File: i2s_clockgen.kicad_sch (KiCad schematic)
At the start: 4 parts, among them U21 24.576MHz, U27 4040

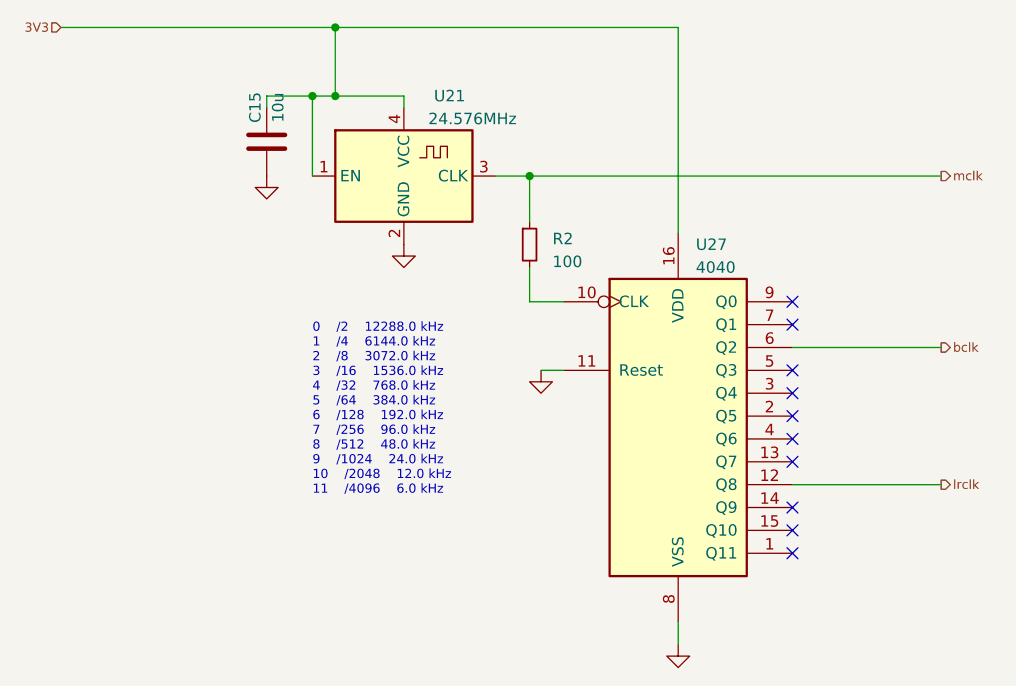
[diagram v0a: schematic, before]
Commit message: update to kicad 8
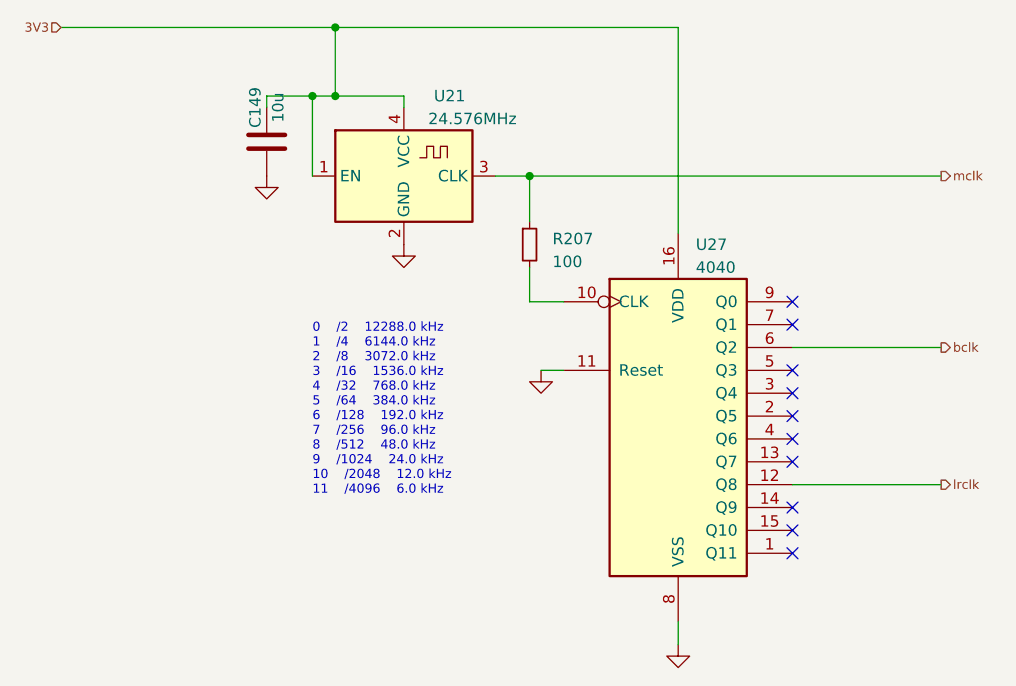
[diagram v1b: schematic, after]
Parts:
- renumbered C15 to C149, R2 to R207

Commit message: updates
* add line out
* fix almost all erc
* some more random edits
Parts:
- U21: PN (none) -> KC2016K24.57C10E
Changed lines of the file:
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@@
 			)
 		)
-		(property "PN" ""
+		(property "PN" "KC2016K24.57C10E"
 			(at 69.85 55.88 0)
 			(effects

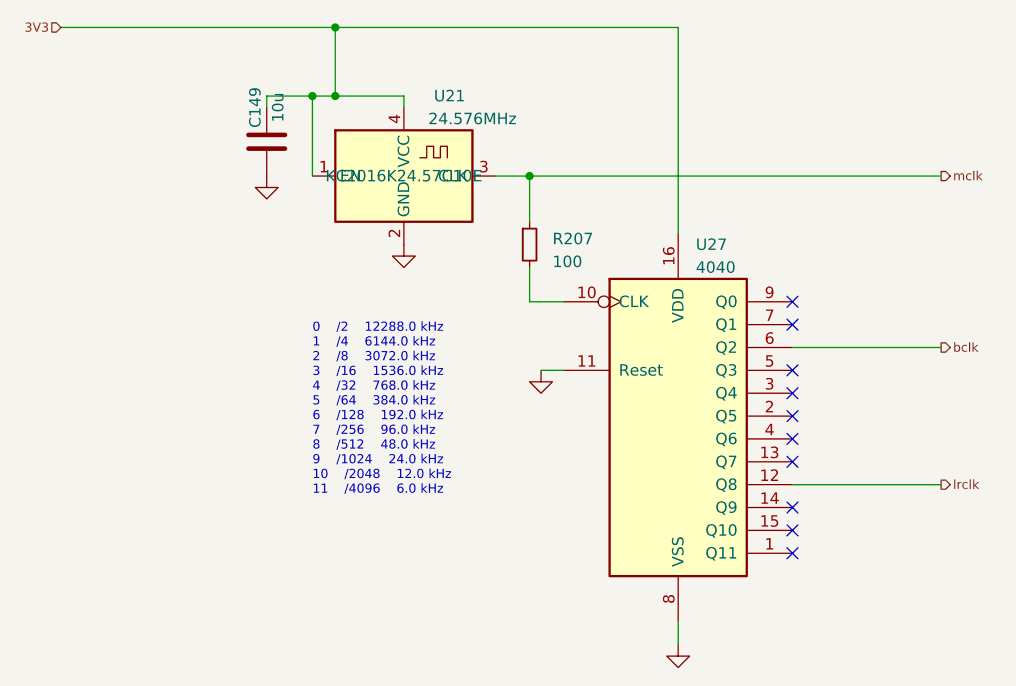
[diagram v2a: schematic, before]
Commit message: add power input +...
+ tons of fixes, footprint assignments, etc
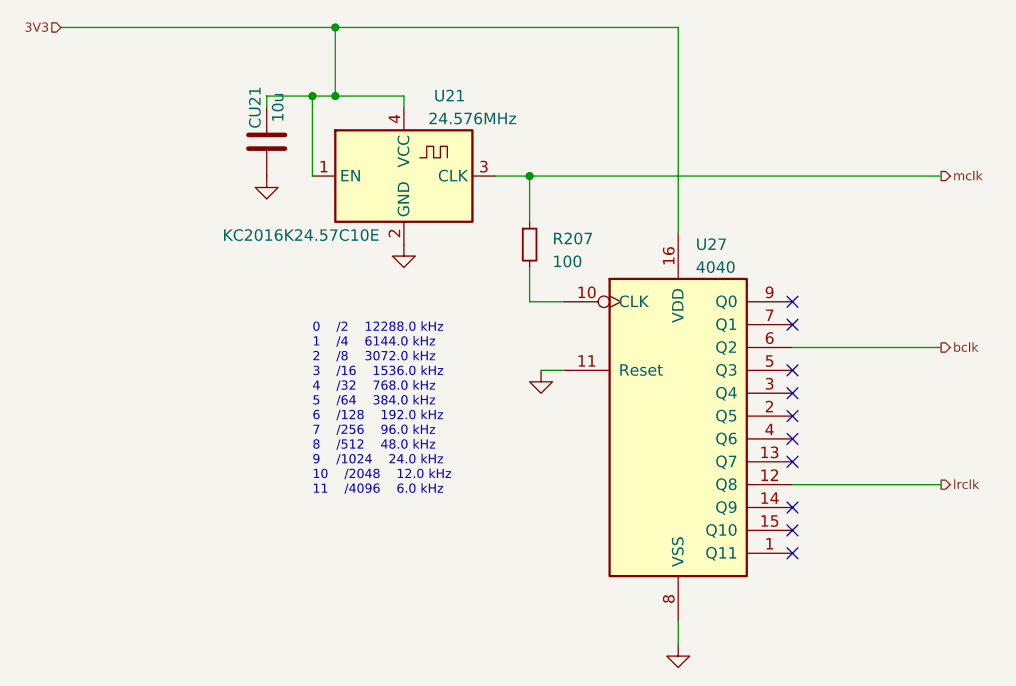
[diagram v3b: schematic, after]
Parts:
- U21: footprint (none) -> invendelirium_audio:K2016_kyocera_xosc
- renumbered C149 to CU21
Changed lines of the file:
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@@
+			)
+		)
+		(property "Sim.Device" ""
+			(at 83.82 63.5 0)
+			(effects
+				(font
+					(size 1.27 1.27)
+				)
+				(hide yes)
+			)
+		)
+		(property "Sim.Library" ""
+			(at 83.82 63.5 0)
+			(effects
+				(font
+					(size 1.27 1.27)
+				)
+				(hide yes)
+			)
+		)
+		(property "Sim.Name" ""
+			(at 83.82 63.5 0)
+			(effects
+				(font
+					(size 1.27 1.27)
+				)
+				(hide yes)
+			)
+		)
+		(property "Sim.Pins" ""
+			(at 83.82 63.5 0)
+			(effects
+				(font
+					(size 1.27 1.27)
+				)
+				(hide yes)
 			)
 		)
@@
 		(on_board yes)
 		(dnp no)
-		(property "Reference" "C149"
+		(property "Reference" "CU21"
 			(at 53.34 48.26 90)
 			(effects
@@
 		)
 		(property "Voltage" "16V"
+			(at 54.61 52.07 0)
+			(effects
+				(font
+					(size 1.27 1.27)
+				)
+				(hide yes)
+			)
+		)
+		(property "Sim.Device" ""
+			(at 54.61 52.07 0)
+			(effects
+				(font
+					(size 1.27 1.27)
+				)
+				(hide yes)
+			)
+		)
+		(property "Sim.Library" ""
+			(at 54.61 52.07 0)
+			(effects
+				(font
+					(size 1.27 1.27)
+				)
+				(hide yes)
+			)
+		)
+		(property "Sim.Name" ""
+			(at 54.61 52.07 0)
+			(effects
+				(font
+					(size 1.27 1.27)
+				)
+				(hide yes)
+			)
+		)
+		(property "Sim.Pins" ""
 			(at 54.61 52.07 0)
 			(effects
@@
 			(project "uberamp1"
 				(path "/310059c1-d84b-43e2-9c9a-0e426c534a12/2fefbd12-b9e0-4841-863e-105a3ff6cb21"
-					(reference "C149")
+					(reference "CU21")
 					(unit 1)
 				)
@@
 			)
 		)
+		(property "Sim.Device" ""
+			(at 100.33 82.55 0)
+			(effects
+				(font
+					(size 1.27 1.27)
+				)
+				(hide yes)
+			)
+		)
+		(property "Sim.Library" ""
+			(at 100.33 82.55 0)
+			(effects
+				(font
+					(size 1.27 1.27)
+				)
+				(hide yes)
+			)
+		)
+		(property "Sim.Name" ""
+			(at 100.33 82.55 0)
+			(effects
+				(font
+					(size 1.27 1.27)
+				)
+				(hide yes)
+			)
+		)
+		(property "Sim.Pins" ""
+			(at 100.33 82.55 0)
+			(effects
+				(font
+					(size 1.27 1.27)
+				)
+				(hide yes)
+			)
+		)
 		(pin "1"
 		)
@@
 			)
 		)
-		(property "Footprint" ""
+		(property "Footprint" "invendelirium_audio:K2016_kyocera_xosc"
 			(at 73.66 52.07 0)
 			(effects
@@
 		)
 		(property "PN" "KC2016K24.57C10E"
+			(at 58.42 62.484 0)
+			(effects
+				(font
+					(size 1.27 1.27)
+				)
+			)
+		)
+		(property "Sim.Device" ""
 			(at 69.85 55.88 0)
 			(effects
@@
 					(size 1.27 1.27)
 				)
-			)
-		)
+				(hide yes)
+			)
+		)
+		(property "Sim.Library" ""
+			(at 69.85 55.88 0)
+			(effects
+				(font
+					(size 1.27 1.27)
+				)
+				(hide yes)
+			)
+		)
+		(property "Sim.Name" ""
+			(at 69.85 55.88 0)
+			(effects
+				(font
+					(size 1.27 1.27)
+				)
+				(hide yes)
+			)
+		)
+		(property "Sim.Pins" ""
+			(at 69.85 55.88 0)
+			(effects
+				(font
+					(size 1.27 1.27)
+				)
+				(hide yes)
+			)
+		)

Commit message: update partnumbers to what was bought
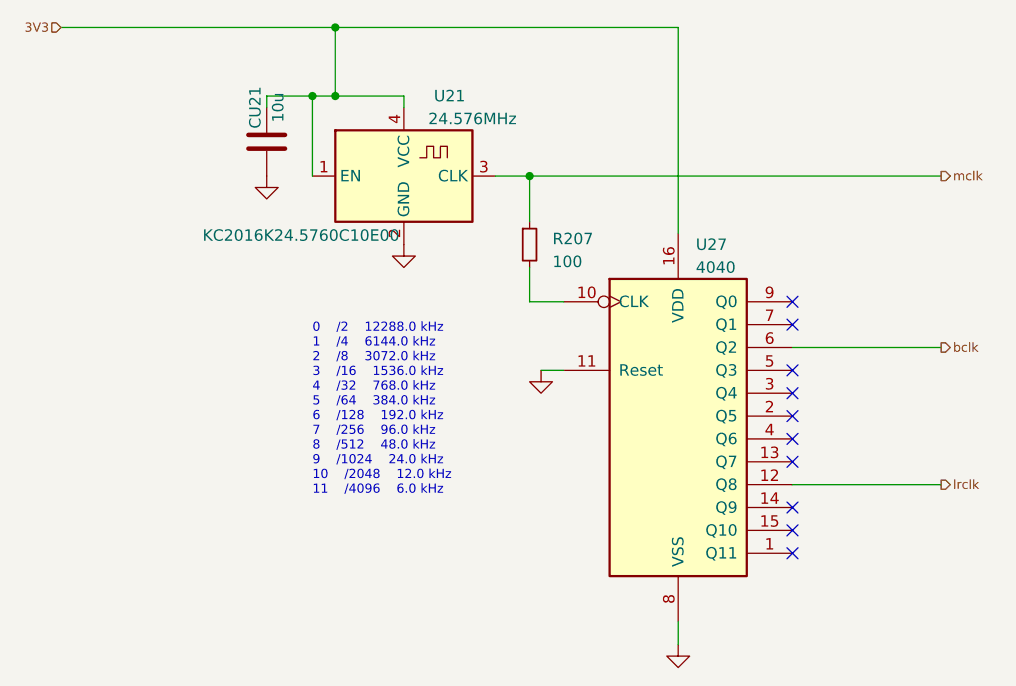
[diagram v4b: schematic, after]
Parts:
- U21: PN KC2016K24.57C10E -> KC2016K24.5760C10E00
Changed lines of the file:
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@@
 			)
 		)
-		(property "PN" "KC2016K24.57C10E"
+		(property "PN" "KC2016K24.5760C10E00"
 			(at 58.42 62.484 0)
 			(effects

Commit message: work on bugs
* align parts
* enlarge cercaps
* fix ak caps
* improve jack footprint
* fix lmr stencil openings
* remove one ldo
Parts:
- CU21: footprint invendelirium_audio:C_0603 -> invendelirium_audio:C_0603_larger
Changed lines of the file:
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@@
 			)
 		)
-		(property "Footprint" "invendelirium_audio:C_0603"
+		(property "Footprint" "invendelirium_audio:C_0603_larger"
 			(at 53.6448 48.26 0)
 			(effects
